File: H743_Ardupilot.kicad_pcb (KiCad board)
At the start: 2 copper layers, 36.5 x 36.5 mm, 155 parts, among them J1 Analog, J10 Led ext, J11 Buzzer, J12 10067099-200LF, J13 Can1_2, J14 Can1_1, J2 Uart1, J3 Uart4, J4 Uart7, J5 Uart(, J6 Uart6, J7 Uart3, J8 I2C1, J9 I2C_2, Q1 AO3400A, U1 USBLC6-2P6, U10 LSM6DSV16X, U11 ICM-45686, U12 BMP581, U13 DPS368XTSA1, U14 SM08B-SRSS-TB(LF)(SN), U2 STM32H743VIT6, U3 LMR43620R5RPER, U4 LMR604303SRAKRQ1, U5 AP7361C-33FGE-7, U6 AP7361C-33FGE-7, U7 TJA1051TK/3,118, U8 SM04B-GHS-TB(LF)(SN), U9 BMI088, Y1 8MHz

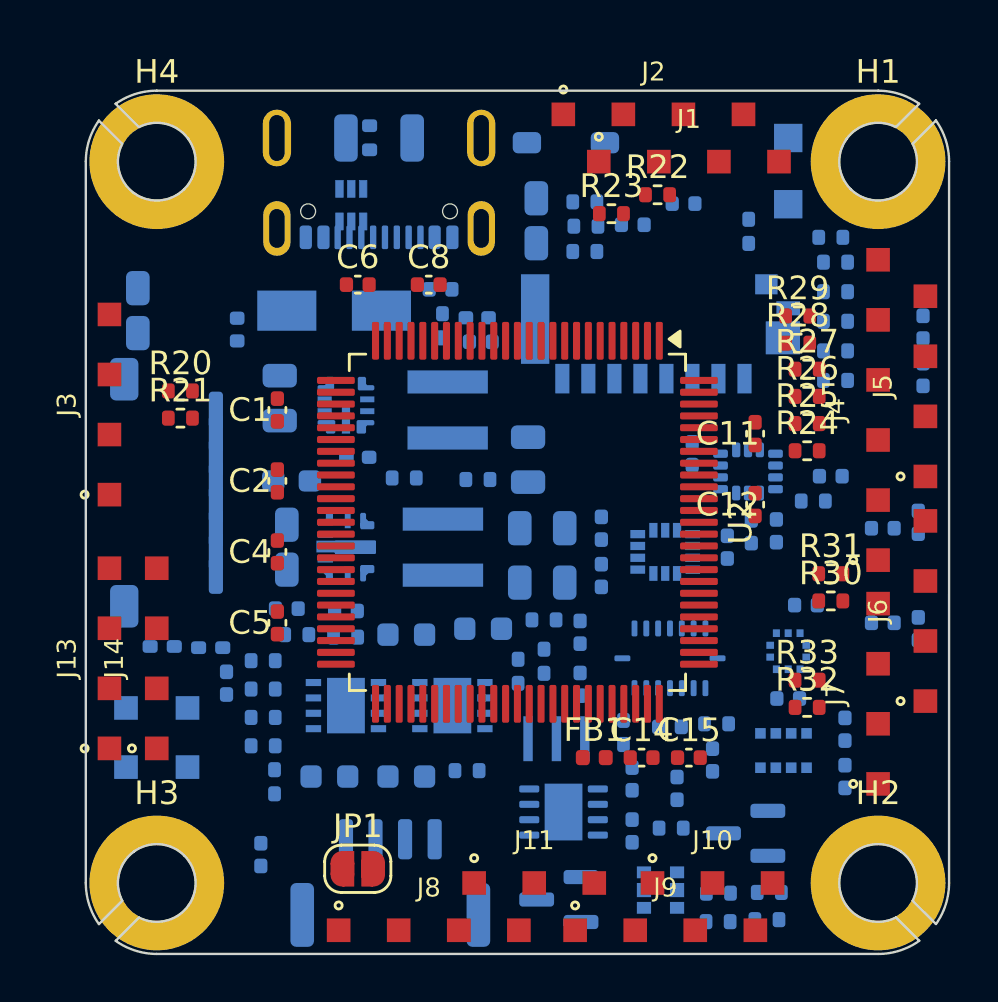
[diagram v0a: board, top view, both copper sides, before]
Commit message: Optimize PCB placement: move power to front, clear USB1 and recess microSD
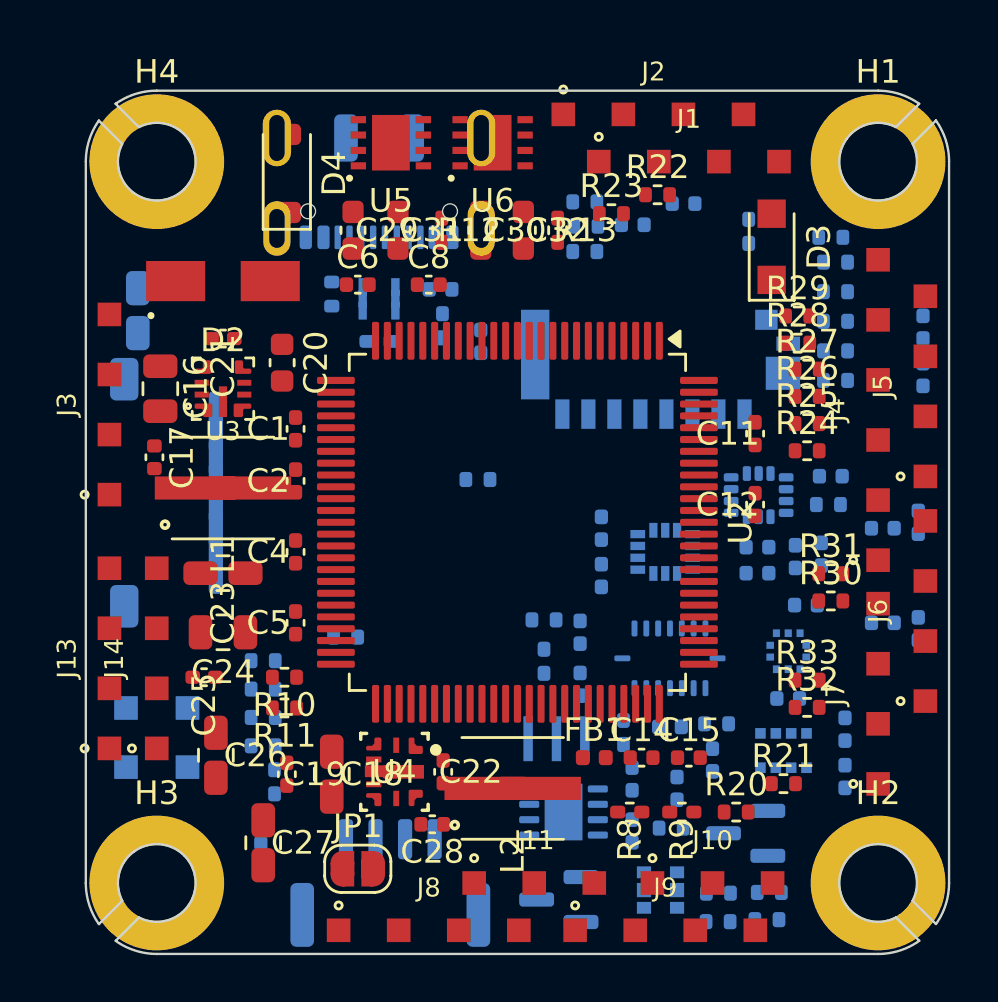
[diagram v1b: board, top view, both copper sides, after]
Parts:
- C16, C17, C18, C19, C20, C21, C22, C23, C24, C25, C26, C27, C28, C29, C30, C31, C32, D2, D3, D4, L1, L2, R10, R11, R12, R13, R8, R9, U3, U4, U5, U6: moved to F.Cu
- moved R21 29.8 mm to (104.0, 114.8)
- moved R20 29.5 mm to (102.0, 116.0)
- moved C32 24.5 mm to (93.0, 91.4), turned to 90 degrees
- moved U5 23.9 mm to (87.4, 87.7), turned to 0 degrees
- moved U6 23.9 mm to (91.7, 87.7), turned to 0 degrees
- moved R13 23.2 mm to (94.5, 91.4), turned to 90 degrees
- moved C31 23.1 mm to (87.7, 91.4), turned to 90 degrees
- moved C24 21.9 mm to (80.3, 108.4), turned to 0 degrees
- moved R9 21.1 mm to (99.7, 116.0), turned to 0 degrees
- moved R8 21.0 mm to (97.5, 116.0), turned to 0 degrees
- moved C25 19.1 mm to (79.5, 110.3)
- moved R12 18.2 mm to (89.5, 91.4), turned to 90 degrees
- moved C29 17.2 mm to (85.8, 91.4), turned to 90 degrees
- moved C30 16.9 mm to (91.2, 91.4), turned to 90 degrees
- moved C26 16.8 mm to (80.0, 113.6), turned to 90 degrees
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
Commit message: Set PCB to 6 copper layers
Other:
- copper layers 2 -> 6
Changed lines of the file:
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@@
 	(layers
 		(0 "F.Cu" signal)
+		(4 "In1.Cu" signal)
+		(6 "In2.Cu" signal)
+		(8 "In3.Cu" signal)
+		(10 "In4.Cu" signal)
 		(2 "B.Cu" signal)
 		(9 "F.Adhes" user "F.Adhesive")

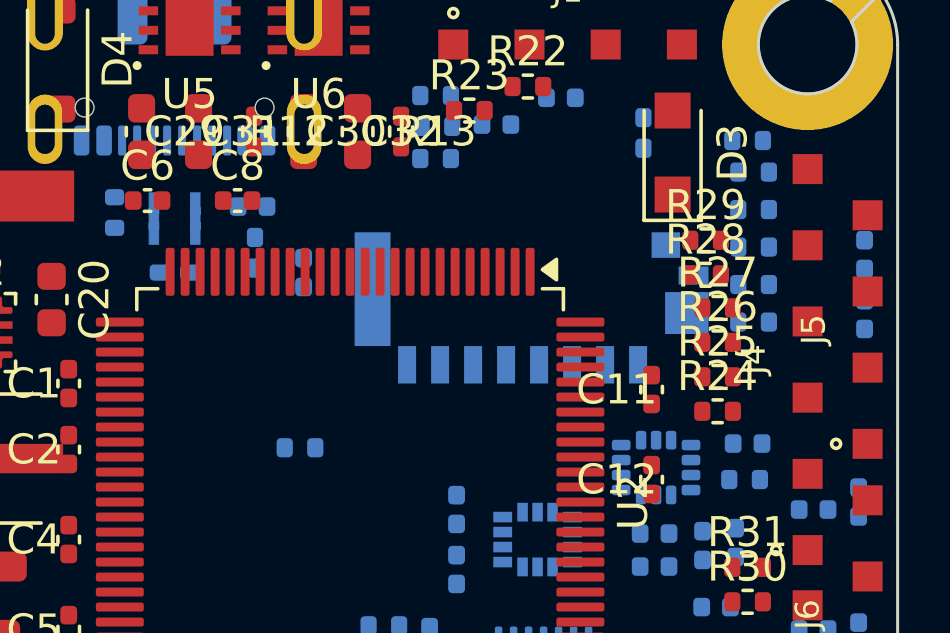
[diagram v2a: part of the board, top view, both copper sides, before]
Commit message: Apply EMC layout review: move VCAPs to top and refresh PCB status
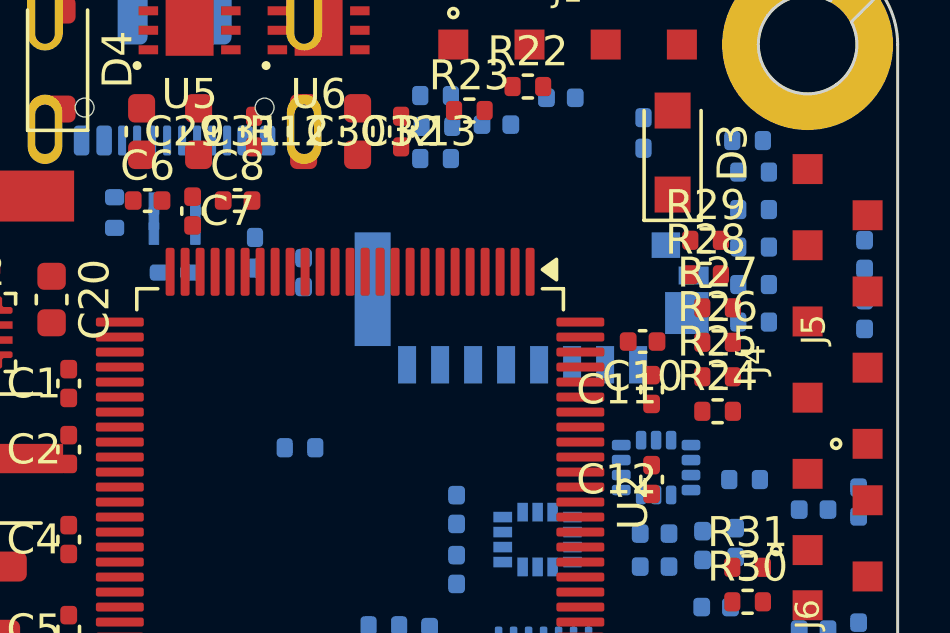
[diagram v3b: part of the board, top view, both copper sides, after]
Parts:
- C10, C7: moved to F.Cu
- moved C10 4.88 mm to (102.5, 98.4), turned to 0 degrees
- moved C7 2.01 mm to (87.5, 94.0), turned to 90 degrees

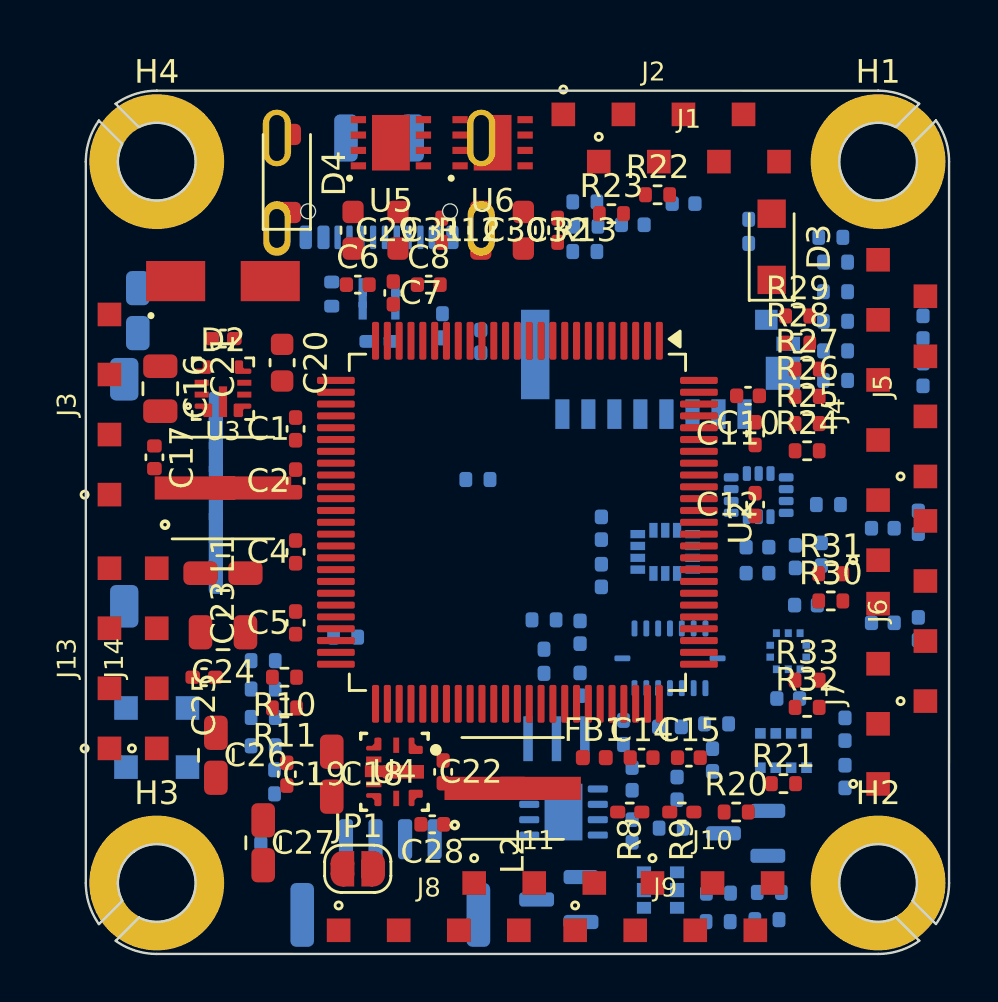
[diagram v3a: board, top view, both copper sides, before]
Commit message: Optimize buck decoupling and 9V feedback placement
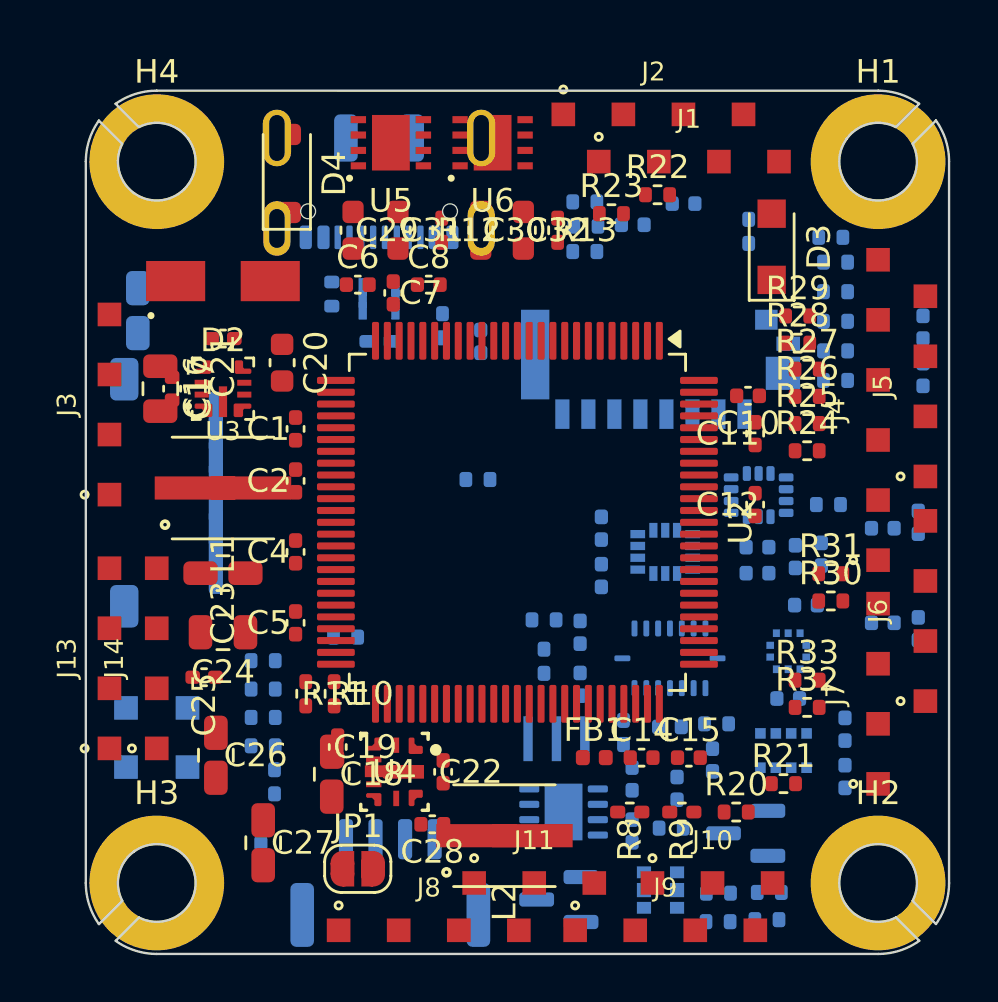
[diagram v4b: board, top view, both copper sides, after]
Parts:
- moved C17 3.00 mm to (78.2, 98.1)
- moved C19 2.44 mm to (85.2, 113.2)
- moved R10 2.21 mm to (85.0, 111.0), turned to 90 degrees
- moved L2 2.03 mm to (92.2, 117.0)
- moved R11 1.08 mm to (83.8, 111.0), turned to 90 degrees
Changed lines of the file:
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@@
 	(footprint "H743_Custom:L_Coilcraft_XGL4030"
 		(layer "F.Cu")
-		(at 92.55 115 0)
+		(at 92.2 117 0)
 		(descr "Coilcraft XGL4030 shielded power inductor; recommended land pattern for Coilcraft XGL4030 series, 4.0 x 4.0 mm body")
 		(tags "Coilcraft XGL4030 power inductor 4x4mm")
@@
 	(footprint "Resistor_SMD:R_0402_1005Metric"
 		(layer "F.Cu")
-		(at 82.9 110.3 0)
+		(at 85 111 90)
 		(descr "Resistor SMD 0402 (1005 Metric), square (rectangular) end terminal, IPC-7351 nominal, (Body size source: IPC-SM-782 page 72, https://www.pcb-3d.com/wordpress/wp-content/uploads/ipc-sm-782a_amendment_1_and_2.pdf)")
 		(tags "resistor")
@@
 	(footprint "Resistor_SMD:R_0402_1005Metric"
 		(layer "F.Cu")
-		(at 82.9 111.6 0)
+		(at 83.8 111 90)
 		(descr "Resistor SMD 0402 (1005 Metric), square (rectangular) end terminal, IPC-7351 nominal, (Body size source: IPC-SM-782 page 72, https://www.pcb-3d.com/wordpress/wp-content/uploads/ipc-sm-782a_amendment_1_and_2.pdf)")
 		(tags "resistor")
@@
 	(footprint "Capacitor_SMD:C_0402_1005Metric"
 		(layer "F.Cu")
-		(at 83 114.4 90)
+		(at 85.15 113.25 90)
 		(descr "Capacitor SMD 0402 (1005 Metric), square (rectangular) end terminal, IPC-7351 nominal, (Body size source: IPC-SM-782 page 76, https://www.pcb-3d.com/wordpress/wp-content/uploads/ipc-sm-782a_amendment_1_and_2.pdf)")
 		(tags "capacitor")
@@
 	(footprint "Capacitor_SMD:C_0402_1005Metric"
 		(layer "F.Cu")
-		(at 77.4 101 90)
+		(at 78.15 98.1 90)
 		(descr "Capacitor SMD 0402 (1005 Metric), square (rectangular) end terminal, IPC-7351 nominal, (Body size source: IPC-SM-782 page 76, https://www.pcb-3d.com/wordpress/wp-content/uploads/ipc-sm-782a_amendment_1_and_2.pdf)")
 		(tags "capacitor")

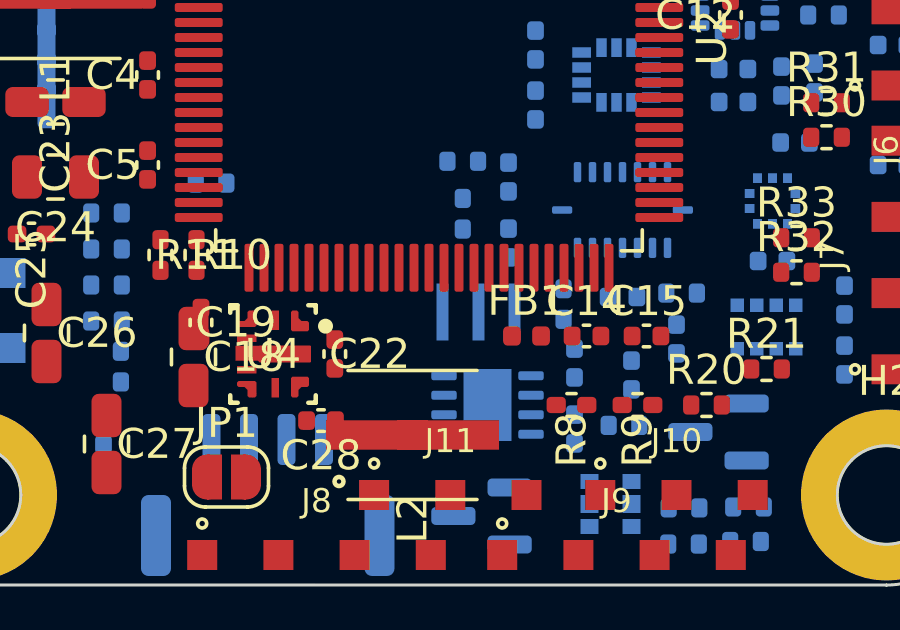
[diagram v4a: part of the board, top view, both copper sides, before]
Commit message: Create oscillator isolation and Bosch MEMS keepouts
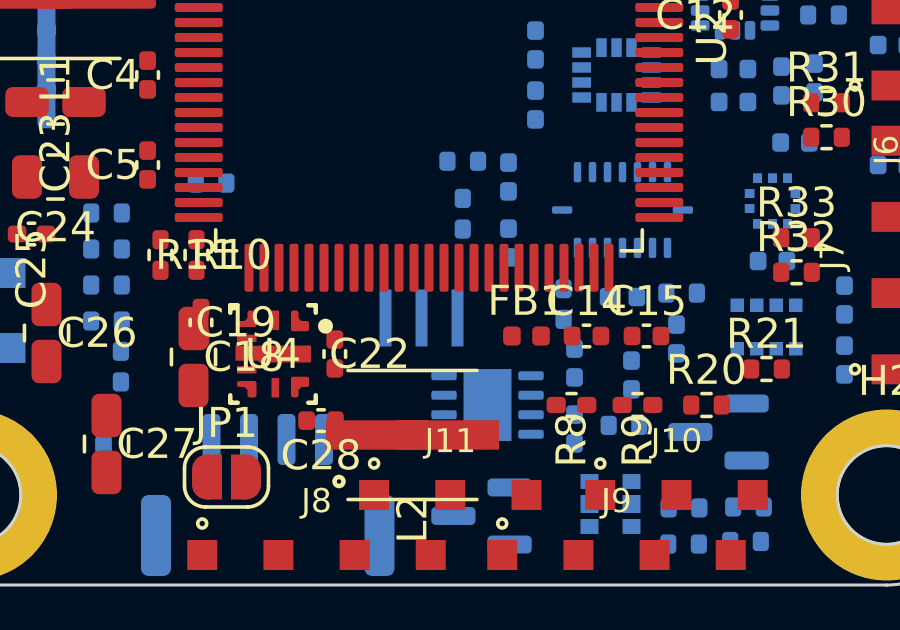
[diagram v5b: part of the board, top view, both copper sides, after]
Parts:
- moved Y1 1.91 mm to (92.5, 113.1)
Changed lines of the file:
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@@
 			(polygon
 				(pts
-					(xy 118.299286 105.2925) (xy 114.949286 105.2925) (xy 114.949286 107.1425) (xy 118.299286 107.1425)
+					(xy -1.5 -2.25) (xy 1.5 -2.25) (xy 1.5 2.25) (xy -1.5 2.25)
 				)
 			)
@@
 			(pinfunction "VDD")
 		)
+		(zone
+			(layer "B.Cu")
+			(name "Bosch BMP581 under-package keepout")
+			(hatch edge 0.25)
+			(connect_pads (clearance 0))
+			(min_thickness 0.1)
+			(keepout
+				(tracks not_allowed)
+				(vias not_allowed)
+				(pads allowed)
+				(copperpour not_allowed)
+				(footprints allowed)
+			)
+			(placement (enabled no) (sheetname ""))
+			(fill (thermal_gap 0.3) (thermal_bridge_width 0.3) (island_removal_mode 0))
+			(polygon
+				(pts
+					(xy -1 -1) (xy 1 -1) (xy 1 1) (xy -1 1)
+				)
+			)
+		)
 		(embedded_fonts no)
 		(model "${KIPRJMOD}/composants/3d/BMP581_envelope.step"
@@
 	(footprint "H743_Custom:Murata_CSTNE_3.2x1.3_P1.2mm"
 		(layer "B.Cu")
-		(at 94.4 112.9 180)
+		(at 92.5 113.1 180)
 		(descr "Murata CSTNE8M00GH5C000R0; JGC42-8858A p3; 0.4 x 1.9 mm lands at 1.2 mm pitch; pin 2 GND.")
 		(property "Reference" "Y1"
@@
 			(pintype "passive")
 		)
+		(zone
+			(layer "B.Cu")
+			(name "OSC local keepout B")
+			(hatch edge 0.25)
+			(connect_pads (clearance 0))
+			(min_thickness 0.1)
+			(keepout
+				(tracks allowed)
+				(vias not_allowed)
+				(pads allowed)
+				(copperpour not_allowed)
+				(footprints allowed)
+			)
+			(placement (enabled no) (sheetname ""))
+			(fill (thermal_gap 0.3) (thermal_bridge_width 0.3) (island_removal_mode 0))
+			(polygon (pts (xy -2 -1.1) (xy 2 -1.1) (xy 2 1.1) (xy -2 1.1)))
+		)
+		(zone
+			(layer "F.Cu")
+			(name "OSC opposite-face keepout F")
+			(hatch edge 0.25)
+			(connect_pads (clearance 0))
+			(min_thickness 0.1)
+			(keepout
+				(tracks not_allowed)
+				(vias not_allowed)
+				(pads not_allowed)
+				(copperpour not_allowed)
+				(footprints not_allowed)
+			)
+			(placement (enabled yes) (sheetname ""))
+			(fill (thermal_gap 0.3) (thermal_bridge_width 0.3) (island_removal_mode 0))
+			(polygon (pts (xy -2.3 -1.4) (xy 2.3 -1.4) (xy 2.3 1.4) (xy -2.3 1.4)))
+		)
 		(embedded_fonts no)

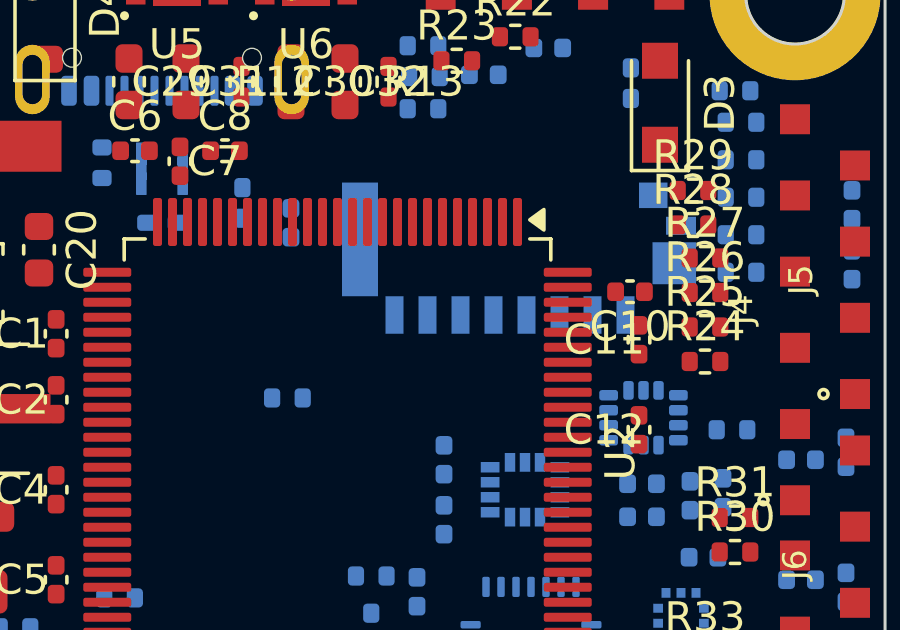
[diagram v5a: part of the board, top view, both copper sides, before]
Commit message: Synchronize SDIO clock series resistor to PCB
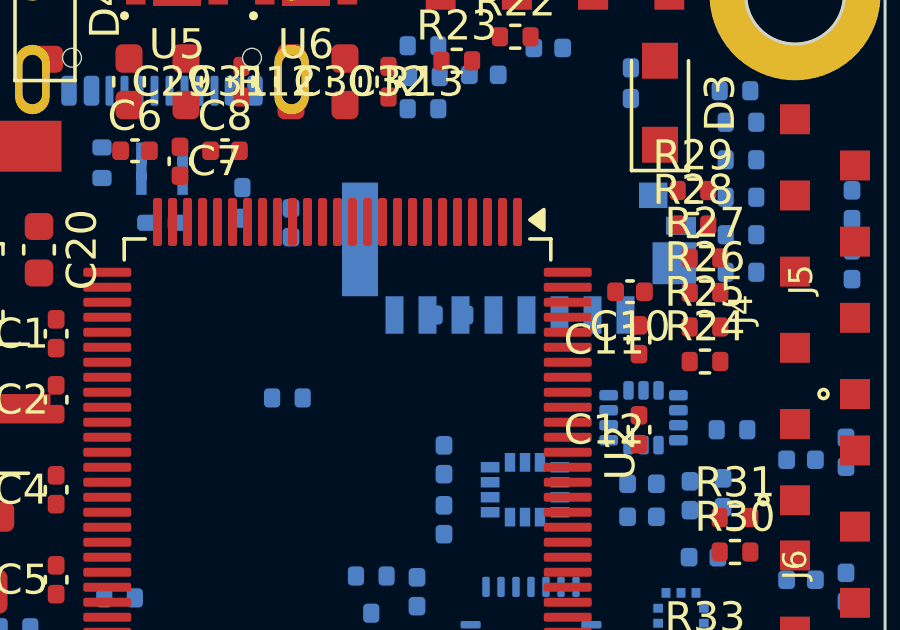
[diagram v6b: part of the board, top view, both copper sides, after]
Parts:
- added R47: 22R, Resistor_SMD:R_0402_1005Metric, B.Cu at (96.5, 99.2)
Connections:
- J12 pad 5: /MICRO_SD/SDIO.CK -> Net-(J12-CLK-Pad5)
